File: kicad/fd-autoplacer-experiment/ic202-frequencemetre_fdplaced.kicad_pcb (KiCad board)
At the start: 2 copper layers, 80 x 50 mm, 49 parts, among them J1 +12V IN (4 pins: 2x+12V, 2x G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, J2 RF IN, J4 LCD, Q1 2SC5551AE-TD-E, U1 AMS1117-5.0, U2 AMS1117 (ADJ), U3 MB506

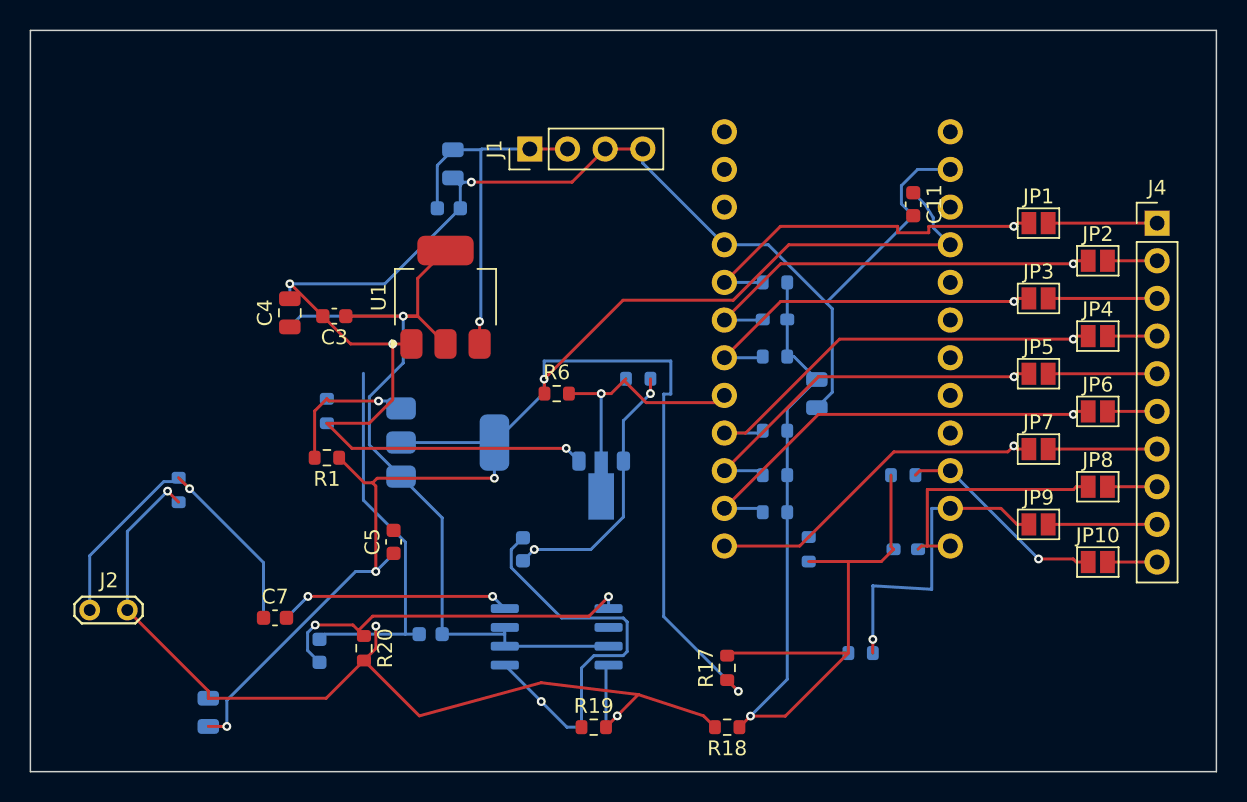
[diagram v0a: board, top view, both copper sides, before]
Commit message: fd-placed : ajustements manuels de placement et routage
Etat verse tel que laisse par l'utilisateur apres ses propres retouches de
placement/routage dans l'editeur KiCad (en parallele du travail d'autoroutage
et de correction DRC mene cote agent sur ce meme board).

Co-Authored-By: Claude Sonnet 5 <noreply@anthropic.com>
Claude-Session: https://claude.ai/code/session_017jkpXZgM5sH1vt8JFfAijf
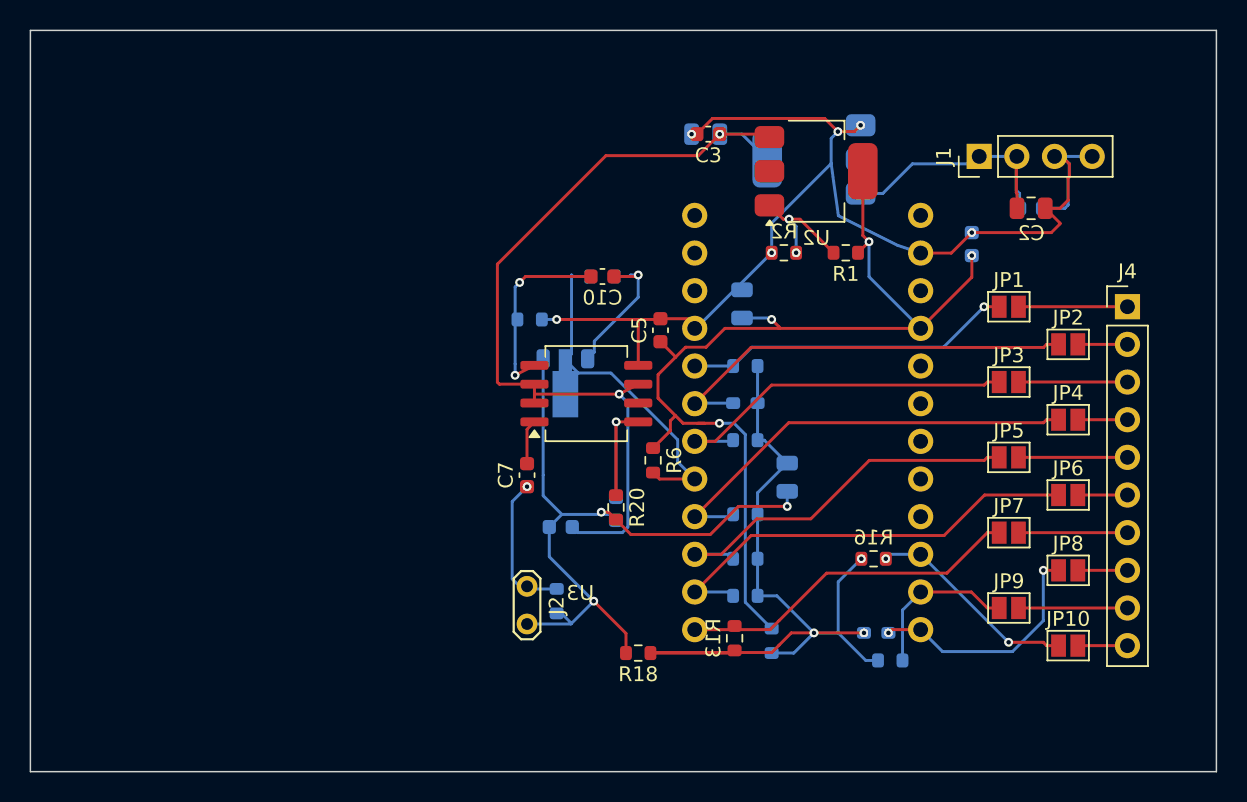
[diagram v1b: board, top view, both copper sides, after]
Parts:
- C10, C11, C2, C4, R13, R16, R17, R19, R2, U1, U2, U3: moved to B.Cu
- moved C6 45.3 mm to (66.0, 35.5)
- moved C1 39.3 mm to (85.5, 29.0)
- moved C2 39.1 mm to (85.5, 29.0), turned to 0 degrees
- moved R1 37.6 mm to (73.0, 32.0)
- moved R2 32.6 mm to (68.8, 32.0), turned to 180 degrees
- moved U2 30.9 mm to (71.0, 26.5)
- moved C4 30.5 mm to (63.5, 24.0), turned to 180 degrees
- moved J1 30.3 mm to (82.0, 25.5)
- moved J2 29.5 mm to (51.5, 54.5), turned to -90 degrees
- moved C3 28.1 mm to (63.7, 24.0)
- moved R19 27.8 mm to (51.7, 36.5)
- moved R3 26.6 mm to (53.5, 55.5)
- moved U1 26.5 mm to (70.8, 25.7), turned to 180 degrees
- moved C5 23.0 mm to (60.5, 37.2)
- moved C8 22.2 mm to (57.5, 49.3), turned to -90 degrees
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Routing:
- net GND: track 198.6 -> 127.9 mm, vias 7 -> 9
- net +3V: track 122.4 -> 68.5 mm, vias 5 -> 4
- net MB506_OUT: track 28.1 -> 12.8 mm, vias 1 -> 2
- net RF_IN: track 24.5 -> 9.92 mm
- net MB506_NIN: track 25.3 -> 11.5 mm, vias 2 -> 1
- net MB506_IN: track 15.7 -> 3.03 mm, vias 2 -> 0
- net VLCD_MID: track 67.2 -> 57.1 mm, vias 1 -> 3
- net LCD_SEG5: track 21.0 -> 10.9 mm, vias 1 -> 0
- net Q1_BASE: track 18.1 -> 10.4 mm, vias 2 -> 1
- net D5_SIG: track 16.5 -> 23.7 mm, vias 1 -> 0
- net +12V: track 25.3 -> 20.1 mm, vias 1 -> 0
- net LCD_COM1: track 25.7 -> 22.2 mm
- net U2_ADJ: track 9.59 -> 8.11 mm, vias 1 -> 2
- net LCD_SEG4: track 17.0 -> 16.4 mm, vias 0 -> 2
- net +5V: track 58.6 -> 58.2 mm, vias 1 -> 2
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
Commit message: Corrige fp-lib-table fd-placed et reroute; ajoute doc LCD
- kicad/fd-autoplacer-experiment/fp-lib-table (nouveau) : enregistre la
  bibliotheque locale "frequencemetre" pour ce sous-projet (jusqu'ici
  invisible faute de fp-lib-table propre a ce dossier -> warning DRC
  "does not include the footprint library 'frequencemetre'").
- fd-placed : reload + effacement + reautoroutage complet (32/32 nets)
  apres application de la correction ci-dessus ; verifie via
  find_wrong_face_stubs.py (0 piste mal orientee). Les etiquettes de face
  incoherentes (lib_footprint_mismatch, 22 cas) etaient deja resolues par
  une sauvegarde depuis l'editeur KiCad entre-temps.
- kicad/frequencemetre.pretty/Arduino_Pro_Mini_Header_2x12.kicad_mod :
  resauvegarde par KiCad 10 (generator_version 9.0 -> 10.0), pas de
  changement fonctionnel (24 pastilles inchangees).
- Reste 1 erreur DRC connue sur fd-placed : chevauchement de courtyard
  C8/R20 (composants places quasi au meme point) - a regler cote
  placement, hors perimetre de ce commit.
- kicad/ic202-frequencemetre.kicad_pcb/.kicad_pro : etat courant de la
  carte principale.
- docs/LCD_2.png : ajout documentation.

Co-Authored-By: Claude Sonnet 5 <noreply@anthropic.com>
Claude-Session: https://claude.ai/code/session_017jkpXZgM5sH1vt8JFfAijf
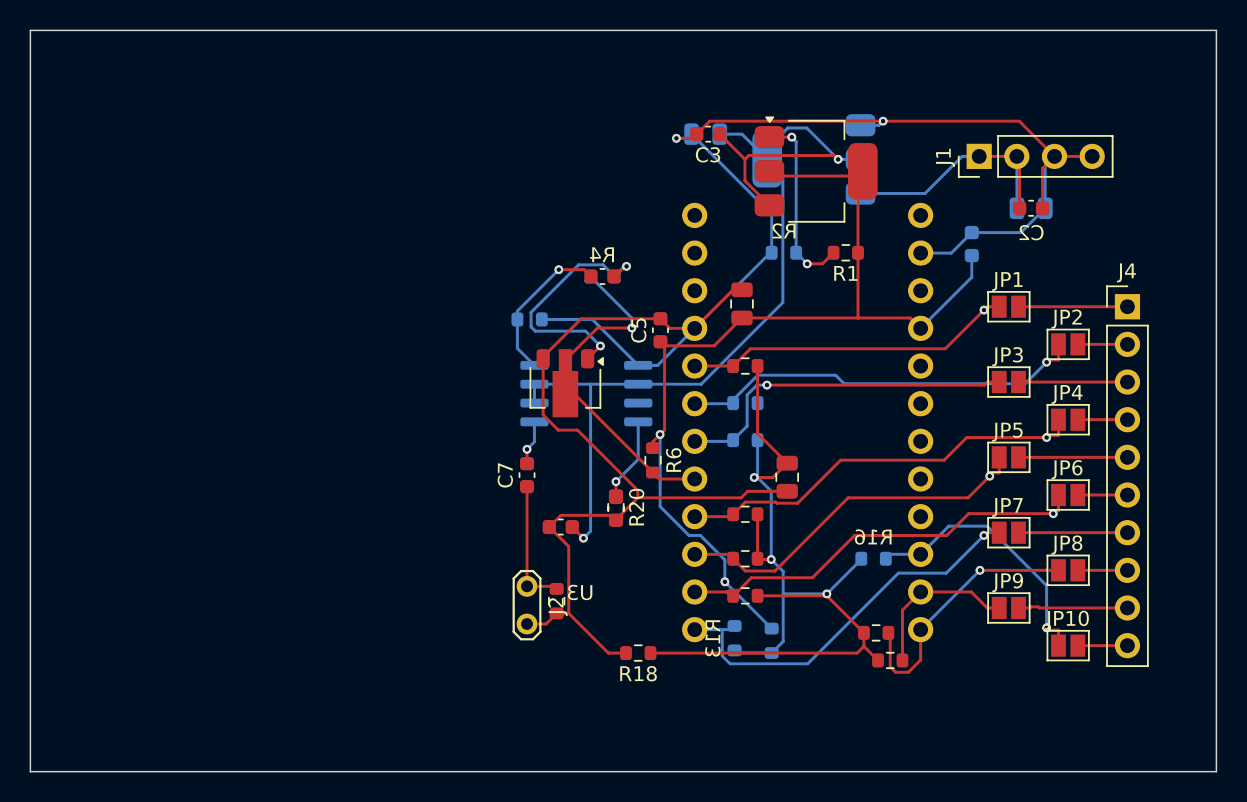
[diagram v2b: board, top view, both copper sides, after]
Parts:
- C10, U2: moved to F.Cu
- R4: moved to B.Cu
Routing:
- net GND: track 127.9 -> 140.2 mm, vias 9 -> 2
- net VLCD_MID: track 57.1 -> 66.1 mm
- net +5V: track 58.2 -> 66.9 mm
- net Q1_BASE: track 10.4 -> 16.9 mm, vias 1 -> 2
- net MB506_NIN: track 11.5 -> 5.72 mm
- net U2_ADJ: track 8.11 -> 12.6 mm
- net LCD_SEG3: track 23.2 -> 27.1 mm, vias 0 -> 1
- net LCD_SEG6: track 14.3 -> 18.2 mm, vias 2 -> 1
- net +3V: track 68.5 -> 65.1 mm, vias 4 -> 2
- net MB506_OUT: track 12.8 -> 10.4 mm, vias 2 -> 1
- net LCD_COM4: track 29.9 -> 27.9 mm, vias 0 -> 1
- net LCD_SEG2: track 29.9 -> 28.4 mm, vias 0 -> 1
- net +12V: track 20.1 -> 18.7 mm
- net LCD_SEG4: track 16.4 -> 17.9 mm, vias 2 -> 1
- net LCD_COM3: track 24.8 -> 23.4 mm, vias 0 -> 1
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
